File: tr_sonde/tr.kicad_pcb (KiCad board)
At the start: 4 copper layers, 104.4 x 65.3 mm, 103 parts, among them J1 SMA, J2 SMA, J3 SMA, K1 TR, K2 HV_MON, K3 VINHDR, Q1 PBSS4250X, Q2 MMBT2222A, Q3 STD2NK90ZT4, Q4 STD2NK90ZT4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

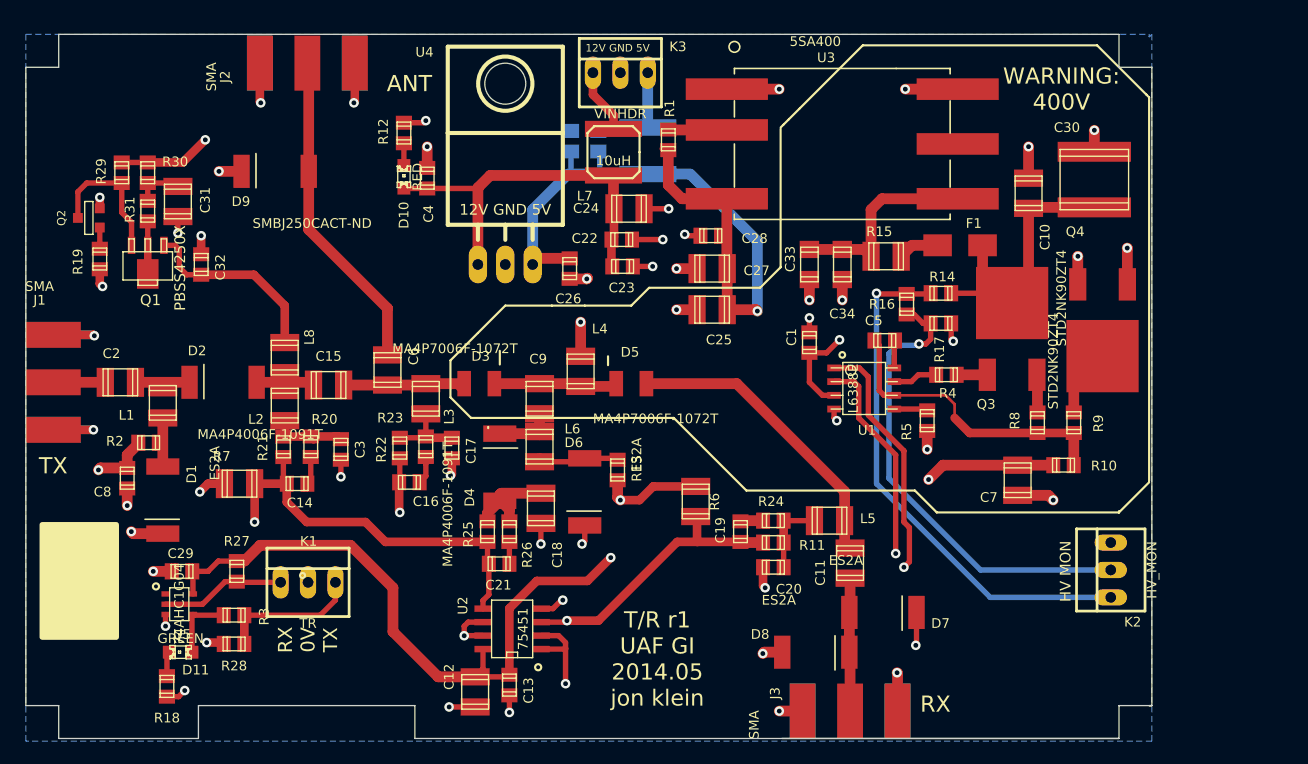
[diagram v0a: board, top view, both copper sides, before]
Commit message: added temperature compensated bias network and heatsink to driver amplifier
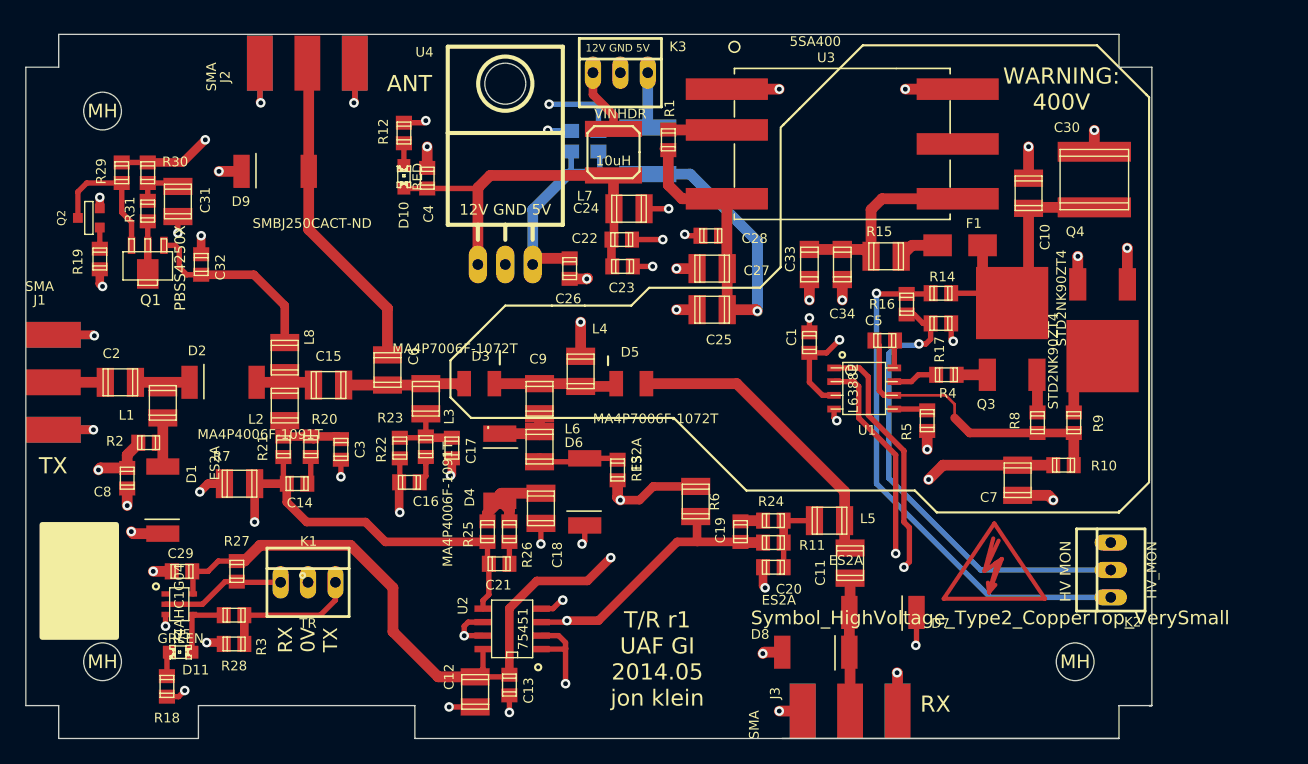
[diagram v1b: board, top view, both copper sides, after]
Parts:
- added ?: Symbol_HighVoltage_Type2_CopperTop_VerySmall, Footprint_Symbols:Symbol_HighVoltage_Type2_CopperTop_VerySmall, F.Cu at (146.9, 74.4)
- added MH: MountingHole_3-5mm_RevA_Date21Jun2010, Mounting_Holes:MountingHole_3-5mm, F.Cu at (64.3, 32.0)
- added MH: MountingHole_3-5mm_RevA_Date21Jun2010, Mounting_Holes:MountingHole_3-5mm, F.Cu at (154.4, 83.1)
- added MH: MountingHole_3-5mm_RevA_Date21Jun2010, Mounting_Holes:MountingHole_3-5mm, F.Cu at (64.3, 83.1)
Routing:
- net GND: track 112.3 -> 134.9 mm, vias 46 -> 48
- removed copper zone on B.Cu, net GND

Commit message: updated tr board to remove DNP components
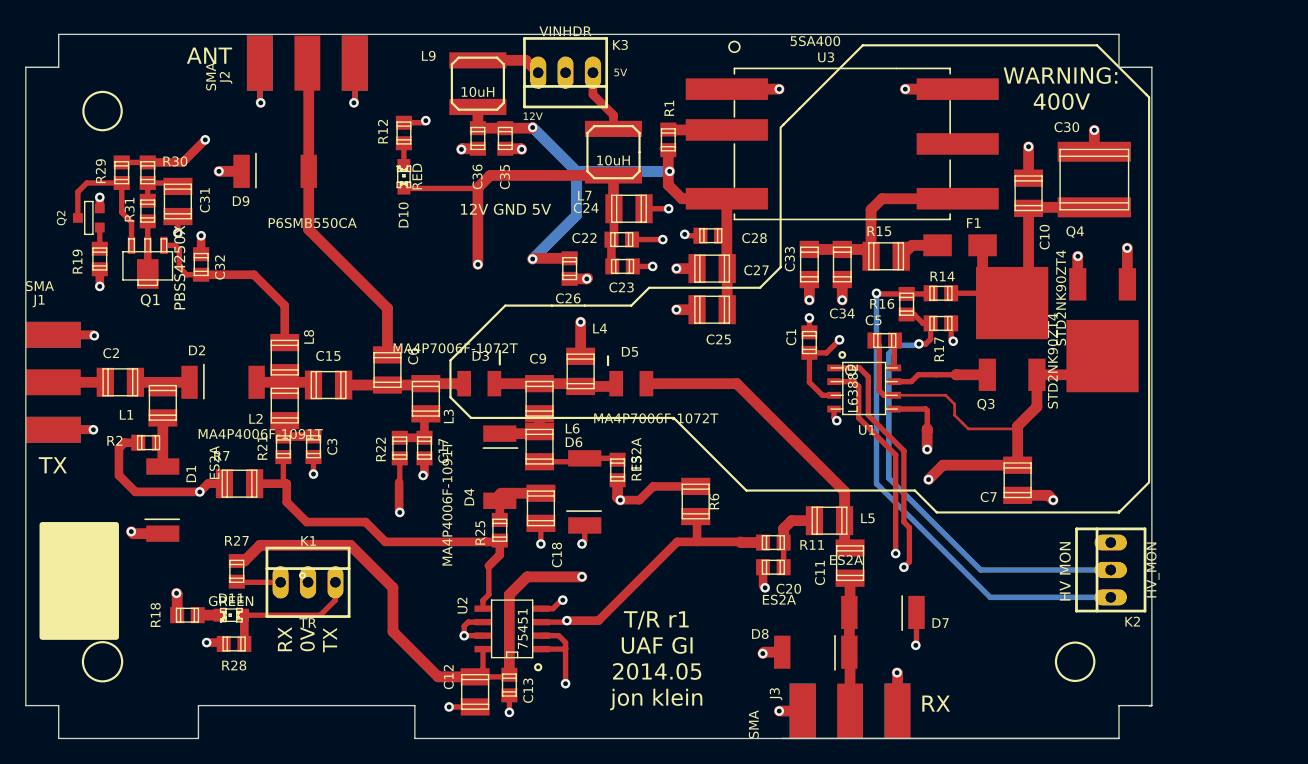
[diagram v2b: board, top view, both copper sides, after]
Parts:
- removed ?: Symbol_HighVoltage_Type2_CopperTop_VerySmall, Footprint_Symbols:Symbol_HighVoltage_Type2_CopperTop_VerySmall
- removed C14, C16, C19, C21, R20, R23, R24, R26, R3: DNP, smd_capacitors:c_0805
- removed C29, C4: 100nF, smd_capacitors:c_0805
- removed C8: 20uF, smd_capacitors:c_0805
- removed MH (x3): MountingHole_3-5mm_RevA_Date21Jun2010, Mounting_Holes:MountingHole_3-5mm
- removed R10, R4, R5, R8, R9: 0, smd_capacitors:c_0805
- removed U4: OKI-78SR-5/1.5-W36H-C, Transistors_TO-220:TO-220_Neutral123_Horizontal_LargePads
- removed U5: 74AHC1G04, SMD_Packages:SOT23-5
- C10: value 4700pF -> 4700pF 600V
- C12: value 20uF -> 22uF
- C15, C2, C6: value .022uF -> .022uF 600 V
- C24: value 10uF -> 22uF
- C25, C27: value 47uF -> 22uF
- C30: value 2.2uF -> .47uF 600V
- C33: value 4700pF -> 4700pF 600 V
- C34: value 4700pF -> .022uF 600V
- C35, C36, L9: moved to F.Cu
- C5: value 68nF -> 68nF 600V
- C9: value .022uF -> .022uF, 600 V
- D9: value SMBJ250CACT-ND -> P6SMB550CA
- R14: value 1M -> 9.09M
- R15: value 90 OHM NTC -> 100 OHM PTC
- R16: value 20k -> 5.1k
- R17: value 20k -> 10k
- R18: value 2k -> 10k
- R6, R7: value 43 -> 300
- moved L9 16.9 mm to (99.1, 29.5)
- moved C36 11.2 mm to (99.1, 34.5), turned to 90 degrees
- moved R18 6.87 mm to (72.1, 78.7), turned to 180 degrees
- moved C35 6.10 mm to (101.6, 34.5), turned to 90 degrees
- moved D11 5.82 mm to (76.2, 78.7)
- moved K3 5.08 mm to (107.2, 28.4), turned to 180 degrees
- moved C3 2.55 mm to (83.8, 63.1)
- moved C17 2.54 mm to (94.1, 63.2)
- moved R25 1.15 mm to (101.1, 70.9)
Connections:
- C5 pad 2: /hvout -> /hvbias
- D11 pad 1: Net-(D11-Pad1) -> /TX
- Q3 pad S: /hvs -> /hvbias
- Q4 pad D: /hvd -> /hvbias
- R19 pad 1: /TXDRV -> /RXDRV
- U1 pad 5: Net-(R5-Pad1) -> Net-(Q4-PadG)
- U1 pad 6: /hvout -> /hvbias
- U1 pad 7: Net-(R4-Pad1) -> Net-(Q3-PadG)
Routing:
- net /RXDRV: track 51.0 -> 98.3 mm, vias 2 -> 3
- net /TXDRV: track 80.7 -> 38.2 mm, vias 2 -> 0
- net /hvbias: track 56.5 -> 92.7 mm
- net /hvout: track 28.0 -> 0.00 mm
- net +5V: track 164.5 -> 146.6 mm, vias 2 -> 4
- net GND: track 134.9 -> 122.7 mm, vias 48 -> 44
- net /RX: track 116.4 -> 108.9 mm
- net Net-(D11-Pad1): track 6.42 -> 0.00 mm
- net /hvd: track 6.33 -> 0.00 mm
- net Net-(Q3-PadG): track 2.84 -> 9.04 mm
- net Net-(Q4-PadG): track 38.8 -> 44.0 mm
- net Net-(R4-Pad1): track 4.14 -> 0.00 mm
- net Net-(C16-Pad2): track 4.02 -> 0.00 mm
- net /hvs: track 3.51 -> 0.00 mm
- net Net-(R5-Pad1): track 3.10 -> 0.00 mm
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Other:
- board text added: "12V"
- board text added: "5V"

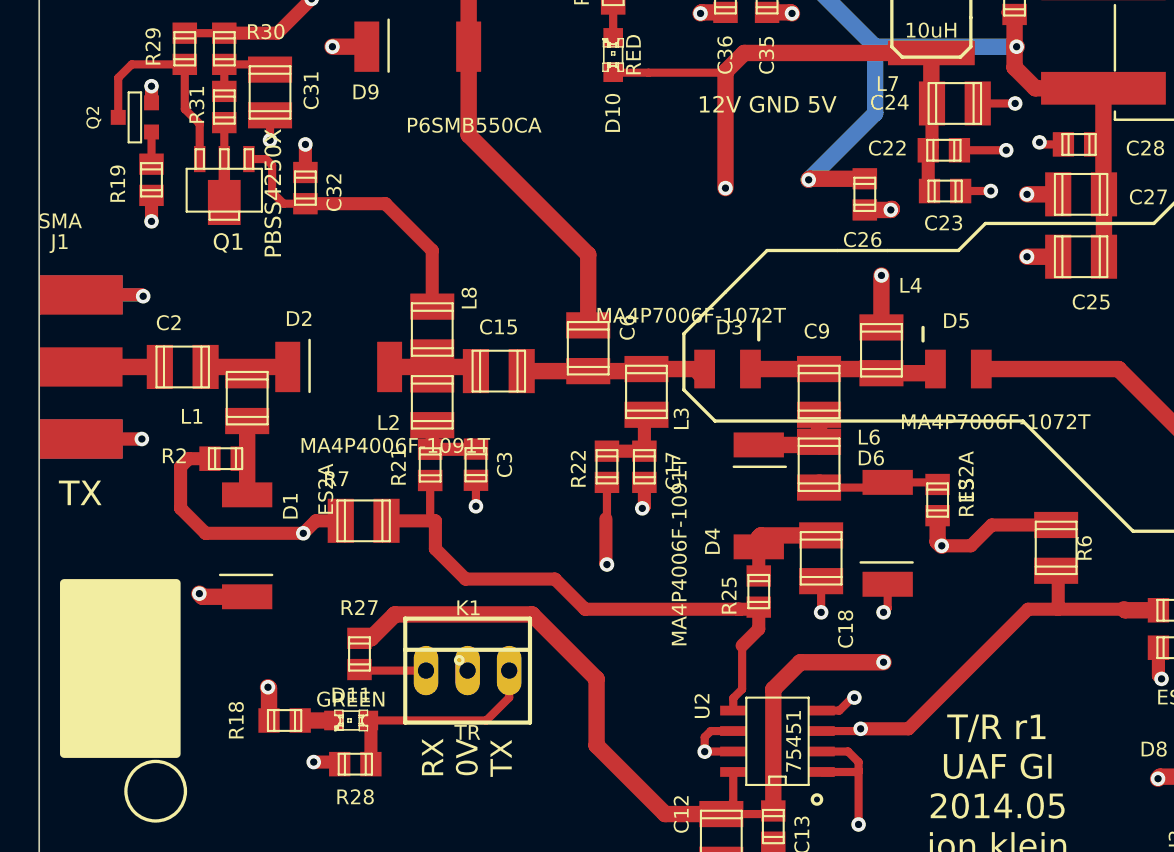
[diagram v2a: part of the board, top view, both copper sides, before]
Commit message: moved agc coupled signal splitting off-board
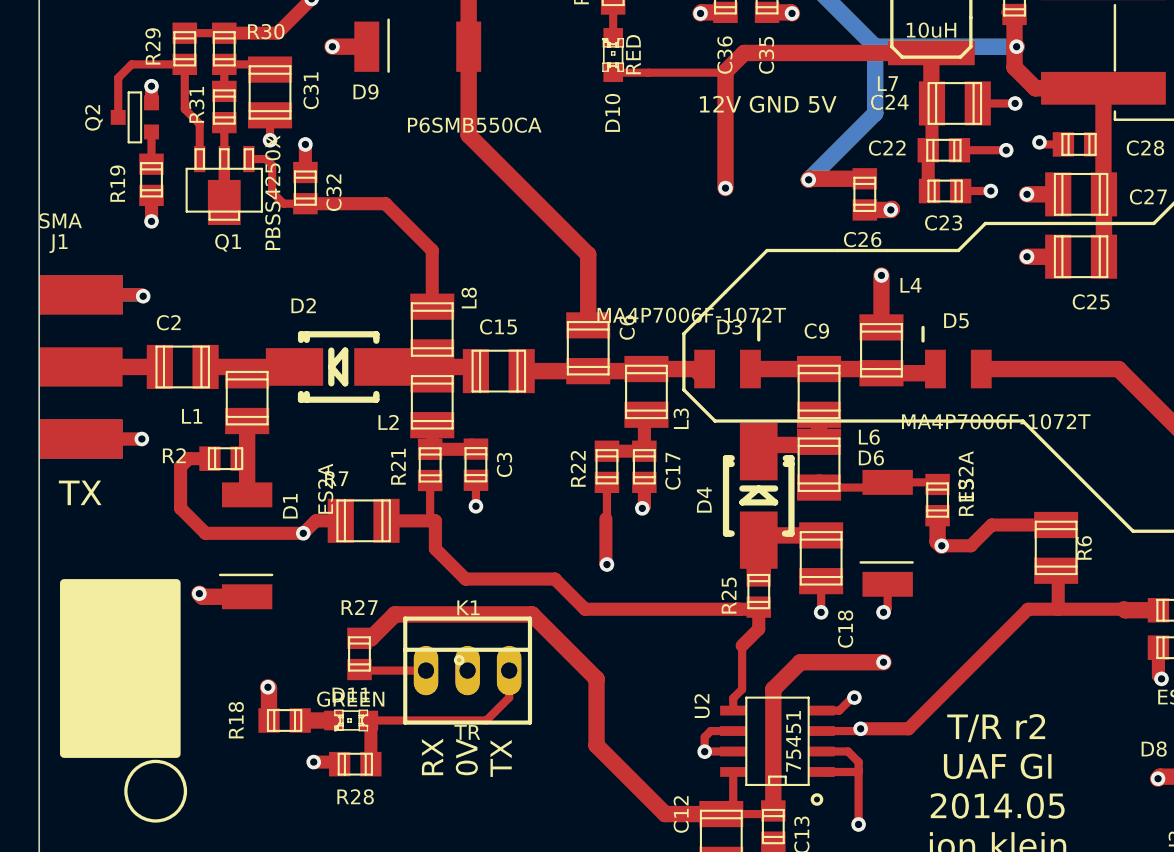
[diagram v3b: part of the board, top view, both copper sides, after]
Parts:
- D2, D4: footprint smb_diode:SMB_DO2144AA -> Diodes_SMD:Diode-SMB_Handsoldering
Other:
- board text added: "T/R r2 UAF GI 2014.05 jon klein"
- board text added: "high power T/R switch r2"
- board text removed: "T/R r1 UAF GI 2014.05 jon klein"
- board text removed: "high power T/R switch r1"

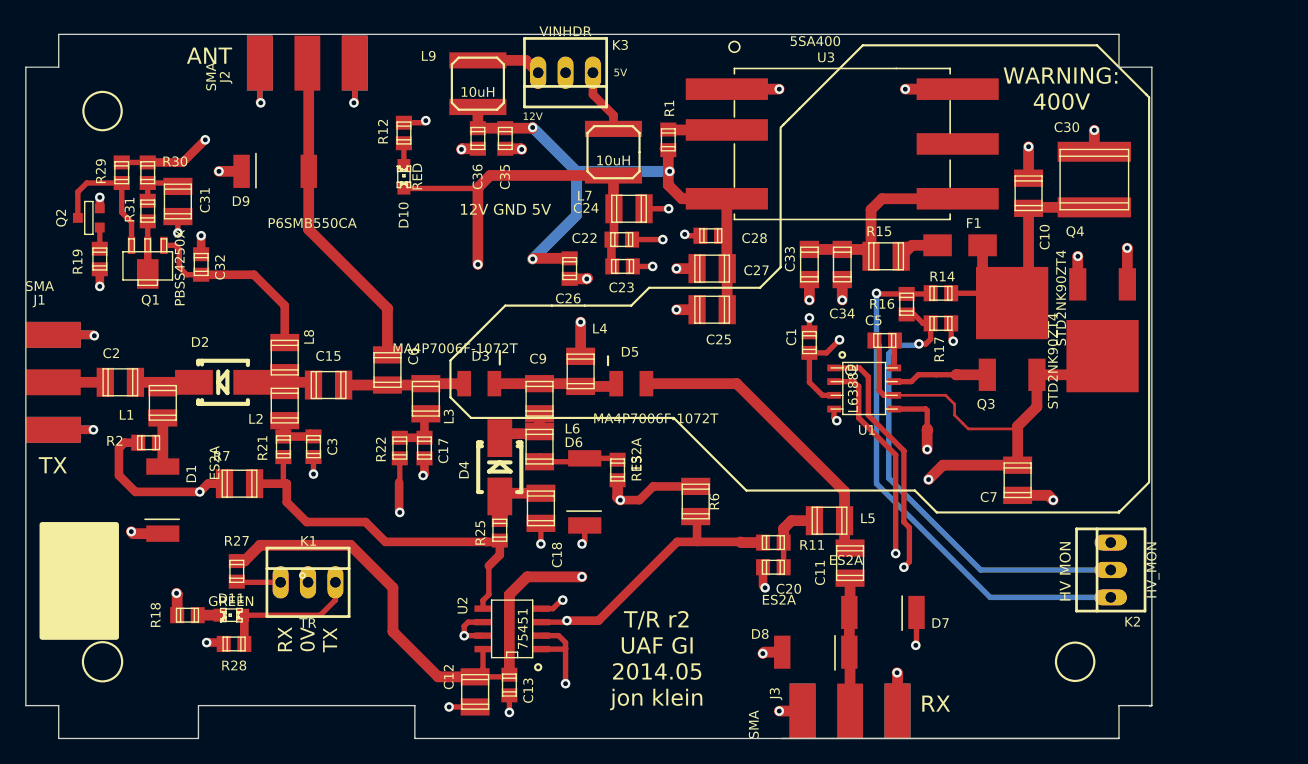
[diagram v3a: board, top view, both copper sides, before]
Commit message: polishing agc, tr, and driver amp for next revisions. moved all bottom layer signal traces to top layer on driver amp
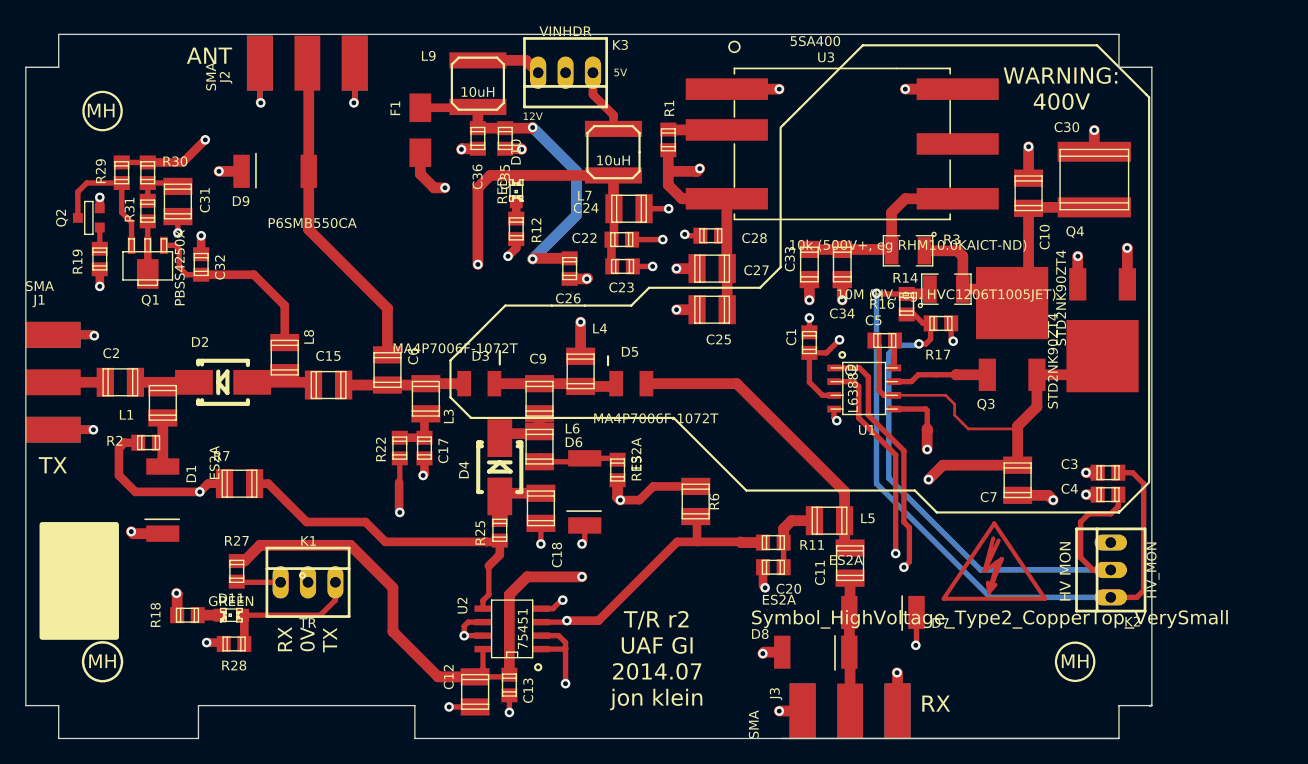
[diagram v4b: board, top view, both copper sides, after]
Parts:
- removed L2: 22uH, smd_capacitors:c_1210
- removed R15: 100 OHM PTC, smd_capacitors:c_1210
- removed R21: 150, smd_capacitors:c_0805
- added ?: Symbol_HighVoltage_Type2_CopperTop_VerySmall, Footprint_Symbols:Symbol_HighVoltage_Type2_CopperTop_VerySmall, F.Cu at (146.9, 74.4)
- added C4: 10nF, smd_capacitors:c_0805, F.Cu at (157.5, 67.6)
- added MH: MountingHole_3-5mm_RevA_Date21Jun2010, Mounting_Holes:MountingHole_3-5mm, F.Cu at (154.4, 83.1)
- added MH: MountingHole_3-5mm_RevA_Date21Jun2010, Mounting_Holes:MountingHole_3-5mm, F.Cu at (64.3, 83.1)
- added MH: MountingHole_3-5mm_RevA_Date21Jun2010, Mounting_Holes:MountingHole_3-5mm, F.Cu at (64.3, 32.0)
- added R3: 10k (500V+, eg RHM10.0KAICT-ND), SMD_Packages:SM1210, F.Cu at (138.9, 45.0)
- C11, C7: value .022uF -> .022uF, 600 V
- F1: value FUSE -> PTC FUSE (0ZCJ0010FF2E)
- R1, R27, R28: value 20k -> 10k
- R12: value 2k -> 10k
- R14: value 9.09M -> 10M (HV, eg. HVC1206T1005JET); footprint smd_capacitors:c_0805 -> SMD_Packages:SM1210
- R16: value 5.1k -> 5k1
- R30: value 200 -> 220
- R6, R7: value 300 -> 300 (1W)
- moved C3 73.7 mm to (157.5, 65.5), turned to 0 degrees
- moved F1 51.2 mm to (93.7, 33.8), turned to 270 degrees
- moved R12 13.7 mm to (102.6, 42.9), turned to 90 degrees
- moved D10 10.5 mm to (102.6, 39.4), turned to 270 degrees
- moved R14 0.64 mm to (142.5, 48.5), turned to 0 degrees
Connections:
- C25 pad 1: +5V -> Net-(C25-Pad1)
- C27 pad 1: +5V -> Net-(C25-Pad1)
- C28 pad 1: +5V -> Net-(C25-Pad1)
- C3 pad 1: GND -> Net-(C3-Pad1)
- C3 pad 2: Net-(C3-Pad2) -> GND
- F1 pad 1: Net-(F1-Pad1) -> +5V
- F1 pad 2: VDD -> Net-(C25-Pad1)
- K2 pad 1: Net-(K2-Pad1) -> Net-(C3-Pad1)
- R1 pad 1: +5V -> Net-(C25-Pad1)
- R14 pad 1: Net-(K2-Pad1) -> Net-(C3-Pad1)
- R16 pad 2: Net-(K2-Pad1) -> Net-(C3-Pad1)
- U3 pad 3: +5V -> Net-(C25-Pad1)
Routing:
- net Net-(C3-Pad1): track 0.00 -> 64.9 mm, vias 0 -> 1
- net Net-(C25-Pad1): track 0.00 -> 55.0 mm, vias 0 -> 2
- net Net-(K2-Pad1): track 48.8 -> 0.00 mm, vias 1 -> 0
- net +5V: track 146.6 -> 120.2 mm, vias 4 -> 3
- net Net-(C4-Pad1): track 44.1 -> 55.9 mm
- net VCC: track 212.4 -> 205.8 mm
- net /TXDRV: track 38.2 -> 32.3 mm
- net Net-(C3-Pad2): track 5.33 -> 0.00 mm
- net VDD: track 35.5 -> 40.1 mm
- net Net-(C15-Pad2): track 12.8 -> 8.76 mm
- net Net-(F1-Pad1): track 3.80 -> 0.00 mm
- net Net-(C33-Pad1): track 18.7 -> 17.9 mm
- net Net-(D10-Pad2): track 2.06 -> 1.55 mm
- net GND: track 122.7 -> 123.0 mm, vias 44 -> 45
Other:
- board text added: "T/R r2 UAF GI 2014.07 jon klein"
- board text removed: "12V GND 5V"
- board text removed: "T/R r2 UAF GI 2014.05 jon klein"
